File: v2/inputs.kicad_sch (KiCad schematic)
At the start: 5 parts

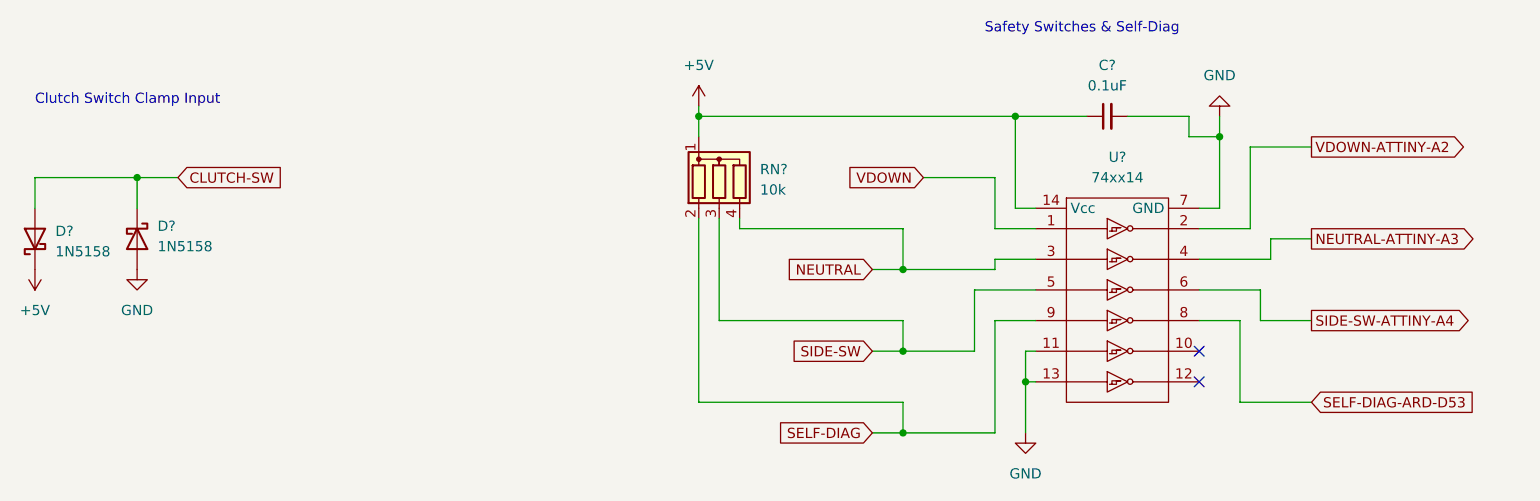
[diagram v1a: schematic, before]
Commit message: update hierarchy
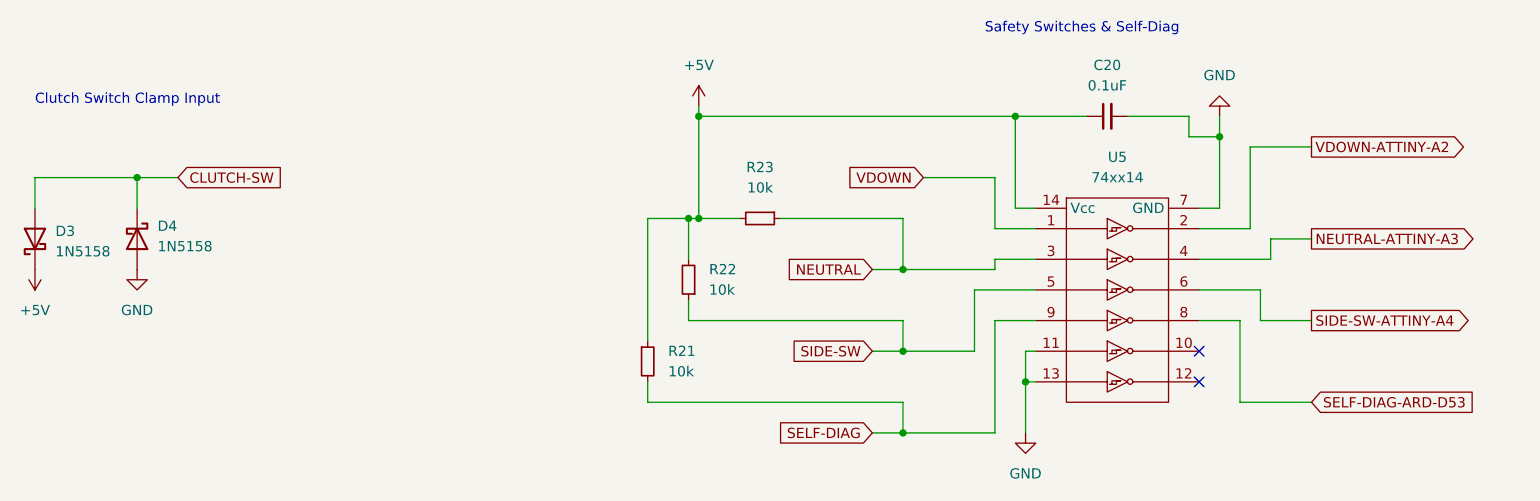
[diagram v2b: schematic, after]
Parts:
- removed RN?: 10k, Resistor_THT:R_Array_SIP4, symbol Device:R_Network03
- added R21, R22, R23: 10k, Resistor_SMD:R_0805_2012Metric, symbol Device:R_Small
- C20: renamed from C?; footprint (none) -> Capacitor_SMD:C_0805_2012Metric
- U5: renamed from U?; footprint (none) -> Package_SO:SOIC-14_3.9x8.7mm_P1.27mm
- gave numbers to parts that had none: 2
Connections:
- net +5V: now also R21.1, R22.2, R23.2
- net NEUTRAL: now also R23.1
- net SELF-DIAG: now also R21.2
- net SIDE-SW: now also R22.1
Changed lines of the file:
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@@
   (junction (at 120.65 34.29) (diameter 0) (color 0 0 0 0)
+  )
+  (junction (at 120.65 46.99) (diameter 0) (color 0 0 0 0)
+  )
+  (junction (at 119.38 46.99) (diameter 0) (color 0 0 0 0)
   )
   (junction (at 146.05 53.34) (diameter 0) (color 0 0 0 0)
@@
     (stroke (width 0) (type default) (color 0 0 0 0))
   )
+  (wire (pts (xy 119.38 46.99) (xy 114.3 46.99))
+    (stroke (width 0) (type default) (color 0 0 0 0))
+  )
   (wire (pts (xy 146.05 69.85) (xy 146.05 73.66))
     (stroke (width 0) (type default) (color 0 0 0 0))
@@
     (stroke (width 0) (type default) (color 0 0 0 0))
   )
-  (wire (pts (xy 125.73 48.26) (xy 146.05 48.26))
+  (wire (pts (xy 119.38 57.15) (xy 119.38 59.69))
     (stroke (width 0) (type default) (color 0 0 0 0))
   )
@@
     (stroke (width 0) (type default) (color 0 0 0 0))
   )
-  (wire (pts (xy 123.19 46.99) (xy 123.19 59.69))
-    (stroke (width 0) (type default) (color 0 0 0 0))
-  )
   (wire (pts (xy 182.88 52.07) (xy 191.77 52.07))
     (stroke (width 0) (type default) (color 0 0 0 0))
@@
     (stroke (width 0) (type default) (color 0 0 0 0))
   )
+  (wire (pts (xy 114.3 46.99) (xy 114.3 62.23))
+    (stroke (width 0) (type default) (color 0 0 0 0))
+  )
   (wire (pts (xy 161.29 63.5) (xy 161.29 67.31))
     (stroke (width 0) (type default) (color 0 0 0 0))
@@
     (stroke (width 0) (type default) (color 0 0 0 0))
   )
-  (wire (pts (xy 120.65 69.85) (xy 146.05 69.85))
+  (wire (pts (xy 114.3 69.85) (xy 146.05 69.85))
     (stroke (width 0) (type default) (color 0 0 0 0))
   )
@@
     (stroke (width 0) (type default) (color 0 0 0 0))
   )
+  (wire (pts (xy 119.38 46.99) (xy 119.38 52.07))
+    (stroke (width 0) (type default) (color 0 0 0 0))
+  )
   (wire (pts (xy 120.65 34.29) (xy 160.02 34.29))
     (stroke (width 0) (type default) (color 0 0 0 0))
@@
     (stroke (width 0) (type default) (color 0 0 0 0))
   )
+  (wire (pts (xy 125.73 46.99) (xy 120.65 46.99))
+    (stroke (width 0) (type default) (color 0 0 0 0))
+  )
   (wire (pts (xy 50.8 41.91) (xy 55.88 41.91))
     (stroke (width 0) (type default) (color 0 0 0 0))
   )
-  (wire (pts (xy 120.65 34.29) (xy 120.65 36.83))
+  (wire (pts (xy 120.65 34.29) (xy 120.65 46.99))
     (stroke (width 0) (type default) (color 0 0 0 0))
   )
@@
     (stroke (width 0) (type default) (color 0 0 0 0))
   )
+  (wire (pts (xy 120.65 46.99) (xy 119.38 46.99))
+    (stroke (width 0) (type default) (color 0 0 0 0))
+  )
   (wire (pts (xy 182.88 48.26) (xy 189.23 48.26))
     (stroke (width 0) (type default) (color 0 0 0 0))
@@
     (stroke (width 0) (type default) (color 0 0 0 0))
   )
-  (wire (pts (xy 123.19 59.69) (xy 146.05 59.69))
+  (wire (pts (xy 119.38 59.69) (xy 146.05 59.69))
+    (stroke (width 0) (type default) (color 0 0 0 0))
+  )
+  (wire (pts (xy 114.3 67.31) (xy 114.3 69.85))
     (stroke (width 0) (type default) (color 0 0 0 0))
   )
@@
     (stroke (width 0) (type default) (color 0 0 0 0))
   )
-  (wire (pts (xy 120.65 46.99) (xy 120.65 69.85))
-    (stroke (width 0) (type default) (color 0 0 0 0))
-  )
-  (wire (pts (xy 125.73 46.99) (xy 125.73 48.26))
+  (wire (pts (xy 130.81 46.99) (xy 146.05 46.99))
     (stroke (width 0) (type default) (color 0 0 0 0))
   )
@@
     (stroke (width 0) (type default) (color 0 0 0 0))
   )
-  (wire (pts (xy 146.05 48.26) (xy 146.05 53.34))
+  (wire (pts (xy 146.05 46.99) (xy 146.05 53.34))
     (stroke (width 0) (type default) (color 0 0 0 0))
   )
@@
     )
   )
+  (symbol (lib_id "Device:R_Small") (at 119.38 54.61 180) (unit 1)
+    (in_bom yes) (on_board yes) (fields_autoplaced)
+    (property "Reference" "R22" (id 0) (at 121.92 53.3399 0)
+      (effects (font (size 1.27 1.27)) (justify right))
+    )
+    (property "Value" "10k" (id 1) (at 121.92 55.8799 0)
+      (effects (font (size 1.27 1.27)) (justify right))
+    )
+    (property "Footprint" "Resistor_SMD:R_0805_2012Metric" (id 2) (at 119.38 54.61 0)
+      (effects (font (size 1.27 1.27)) hide)
+    )
+    (property "Datasheet" "~" (id 3) (at 119.38 54.61 0)
+      (effects (font (size 1.27 1.27)) hide)
+    )
+    (pin "1")
+    (pin "2")
+  )
+  (symbol (lib_id "Device:R_Small") (at 114.3 64.77 0) (unit 1)
+    (in_bom yes) (on_board yes) (fields_autoplaced)
+    (property "Reference" "R21" (id 0) (at 116.84 63.4999 0)
+      (effects (font (size 1.27 1.27)) (justify left))
+    )
+    (property "Value" "10k" (id 1) (at 116.84 66.0399 0)
+      (effects (font (size 1.27 1.27)) (justify left))
+    )
+    (property "Footprint" "Resistor_SMD:R_0805_2012Metric" (id 2) (at 114.3 64.77 0)
+      (effects (font (size 1.27 1.27)) hide)
+    )
+    (property "Datasheet" "~" (id 3) (at 114.3 64.77 0)
+      (effects (font (size 1.27 1.27)) hide)
+    )
+    (pin "1")
+    (pin "2")
+  )
   (symbol (lib_id "power:+5V") (at 120.65 33.02 0) (unit 1)
     (in_bom yes) (on_board yes) (fields_autoplaced)
-    (property "Reference" "#PWR?" (id 0) (at 120.65 36.83 0)
+    (property "Reference" "#PWR030" (id 0) (at 120.65 36.83 0)
       (effects (font (size 1.27 1.27)) hide)
     )
@@
   (symbol (lib_id "mega_2560:74xx14") (at 172.72 64.77 0) (unit 1)
     (in_bom yes) (on_board yes) (fields_autoplaced)
-    (property "Reference" "U?" (id 0) (at 172.72 39.37 0))
+    (property "Reference" "U5" (id 0) (at 172.72 39.37 0))
     (property "Value" "74xx14" (id 1) (at 172.72 41.91 0))
-    (property "Footprint" "" (id 2) (at 172.72 66.04 0)
+    (property "Footprint" "Package_SO:SOIC-14_3.9x8.7mm_P1.27mm" (id 2) (at 172.72 66.04 0)
       (effects (font (size 1.27 1.27)) hide)
     )
@@
   (symbol (lib_id "power:GND") (at 161.29 73.66 0) (unit 1)
     (in_bom yes) (on_board yes) (fields_autoplaced)
-    (property "Reference" "#PWR?" (id 0) (at 161.29 80.01 0)
+    (property "Reference" "#PWR031" (id 0) (at 161.29 80.01 0)
       (effects (font (size 1.27 1.27)) hide)
     )
@@
   (symbol (lib_id "power:GND") (at 185.42 34.29 180) (unit 1)
     (in_bom yes) (on_board yes) (fields_autoplaced)
-    (property "Reference" "#PWR?" (id 0) (at 185.42 27.94 0)
+    (property "Reference" "#PWR032" (id 0) (at 185.42 27.94 0)
       (effects (font (size 1.27 1.27)) hide)
     )
@@
   (symbol (lib_id "Device:D_Schottky") (at 38.1 49.53 90) (unit 1)
     (in_bom yes) (on_board yes) (fields_autoplaced)
-    (property "Reference" "D?" (id 0) (at 40.64 48.5774 90)
+    (property "Reference" "D3" (id 0) (at 40.64 48.5774 90)
       (effects (font (size 1.27 1.27)) (justify right))
     )
@@
     (pin "2")
   )
-  (symbol (lib_id "Device:R_Network03") (at 123.19 41.91 0) (unit 1)
-    (in_bom yes) (on_board yes) (fields_autoplaced)
-    (property "Reference" "RN?" (id 0) (at 128.27 40.8939 0)
-      (effects (font (size 1.27 1.27)) (justify left))
-    )
-    (property "Value" "10k" (id 1) (at 128.27 43.4339 0)
-      (effects (font (size 1.27 1.27)) (justify left))
-    )
-    (property "Footprint" "Resistor_THT:R_Array_SIP4" (id 2) (at 130.175 41.91 90)
-      (effects (font (size 1.27 1.27)) hide)
-    )
-    (property "Datasheet" "http://www.vishay.com/docs/31509/csc.pdf" (id 3) (at 123.19 41.91 0)
-      (effects (font (size 1.27 1.27)) hide)
-    )
-    (pin "1")
-    (pin "2")
-    (pin "3")
-    (pin "4")
+  (symbol (lib_id "Device:R_Small") (at 128.27 46.99 270) (unit 1)
+    (in_bom yes) (on_board yes) (fields_autoplaced)
+    (property "Reference" "R23" (id 0) (at 128.27 40.64 90))
+    (property "Value" "10k" (id 1) (at 128.27 43.18 90))
+    (property "Footprint" "Resistor_SMD:R_0805_2012Metric" (id 2) (at 128.27 46.99 0)
+      (effects (font (size 1.27 1.27)) hide)
+    )
+    (property "Datasheet" "~" (id 3) (at 128.27 46.99 0)
+      (effects (font (size 1.27 1.27)) hide)
+    )
+    (pin "1")
+    (pin "2")
   )
   (symbol (lib_id "power:GND") (at 50.8 53.34 0) (unit 1)
     (in_bom yes) (on_board yes) (fields_autoplaced)
-    (property "Reference" "#PWR?" (id 0) (at 50.8 59.69 0)
+    (property "Reference" "#PWR029" (id 0) (at 50.8 59.69 0)
       (effects (font (size 1.27 1.27)) hide)
     )
@@
   (symbol (lib_id "power:+5V") (at 38.1 53.34 180) (unit 1)
     (in_bom yes) (on_board yes) (fields_autoplaced)
-    (property "Reference" "#PWR?" (id 0) (at 38.1 49.53 0)
+    (property "Reference" "#PWR028" (id 0) (at 38.1 49.53 0)
       (effects (font (size 1.27 1.27)) hide)
     )
@@
   (symbol (lib_id "Device:D_Schottky") (at 50.8 49.53 270) (unit 1)
     (in_bom yes) (on_board yes) (fields_autoplaced)
-    (property "Reference" "D?" (id 0) (at 53.34 47.9424 90)
+    (property "Reference" "D4" (id 0) (at 53.34 47.9424 90)
       (effects (font (size 1.27 1.27)) (justify left))
     )
@@
   (symbol (lib_id "Device:C_Small") (at 171.45 34.29 90) (unit 1)
     (in_bom yes) (on_board yes) (fields_autoplaced)
-    (property "Reference" "C?" (id 0) (at 171.4563 27.94 90))
+    (property "Reference" "C20" (id 0) (at 171.4563 27.94 90))
     (property "Value" "0.1uF" (id 1) (at 171.4563 30.48 90))
-    (property "Footprint" "" (id 2) (at 171.45 34.29 0)
-      (effects (font (size 1.27 1.27)) hide)
-    )
+    (property "Footprint" "Capacitor_SMD:C_0805_2012Metric" (id 2) (at 171.45 34.29 0)
+      (effects (font (size 1.27 1.27)) hide)
+    )
